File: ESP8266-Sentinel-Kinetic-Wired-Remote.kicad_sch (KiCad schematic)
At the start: 41 parts, among them J1 Conn_01x04_Socket, SW1 SW_Push, SW2 SW_Push, SW3 SW_Push, SW4 SW_Push, SW5 SW_Push, U1 AMS1117-3.3, U2 ESP-12F

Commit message: Layed out PCB and created 3D printable enclosure
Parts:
- removed DS?: WC1602A, Display:LCD-016N002L, symbol Display_Character:WC1602A
- added DS1: WC1602A, Display:WC1602A, symbol Display_Character:WC1602A
- added H1, H2, H3, H4: MountingHole, MountingHole:MountingHole_3.2mm_M3, symbol Mechanical:MountingHole
- added RV2: 5K, Potentiometer_THT:Potentiometer_ACP_CA14V-15_Vertical, symbol Device:R_Potentiometer
- J1: now not fitted; now left out of the parts list
- J3: renamed from J?; now not fitted; now left out of the parts list
- RV1: renamed from RV?; footprint Potentiometer_THT:Potentiometer_ACP_CA14V-15_Vertical -> Potentiometer_THT:Potentiometer_Runtron_RM-065_Vertical
- gave numbers to parts that had none: 6
- renumbered SW4 to SW1, SW1 to SW4
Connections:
- net +5V: now also J2.1 (Pin_1), DS1.2 (VDD), RV2.1
- net GND: now also J2.4 (Pin_4), DS1.1 (VSS), RV2.3
- net RS232_RX: now also J2.2 (Pin_2)
- net RS232_TX: now also J2.3 (Pin_3)
- net at U4.16 (P4): now also DS1.11 (D4)
- net at U4.17 (P5): now also DS1.12 (D5)
- net at U4.19 (P6): now also DS1.13 (D6)
- net at U4.20 (P7): now also DS1.14 (D7)
- net at JP4.1 (A): now also DS1.15 (LED(+))
- net at Q1.3 (D): now also DS1.16 (LED(-))
- net at RV1.2: now also DS1.3 (VO), RV2.2
- net at U4.10 (P0): now also DS1.4 (RS)
- net at U4.11 (P1): now also DS1.5 (R/W)
- net at U4.12 (P2): now also DS1.6 (E)
- net A0: no longer names the net of U2.2 (ADC)
- net GPIO16: no longer names the net of U2.4 (GPIO16)
- no-connect marks 13 -> 15

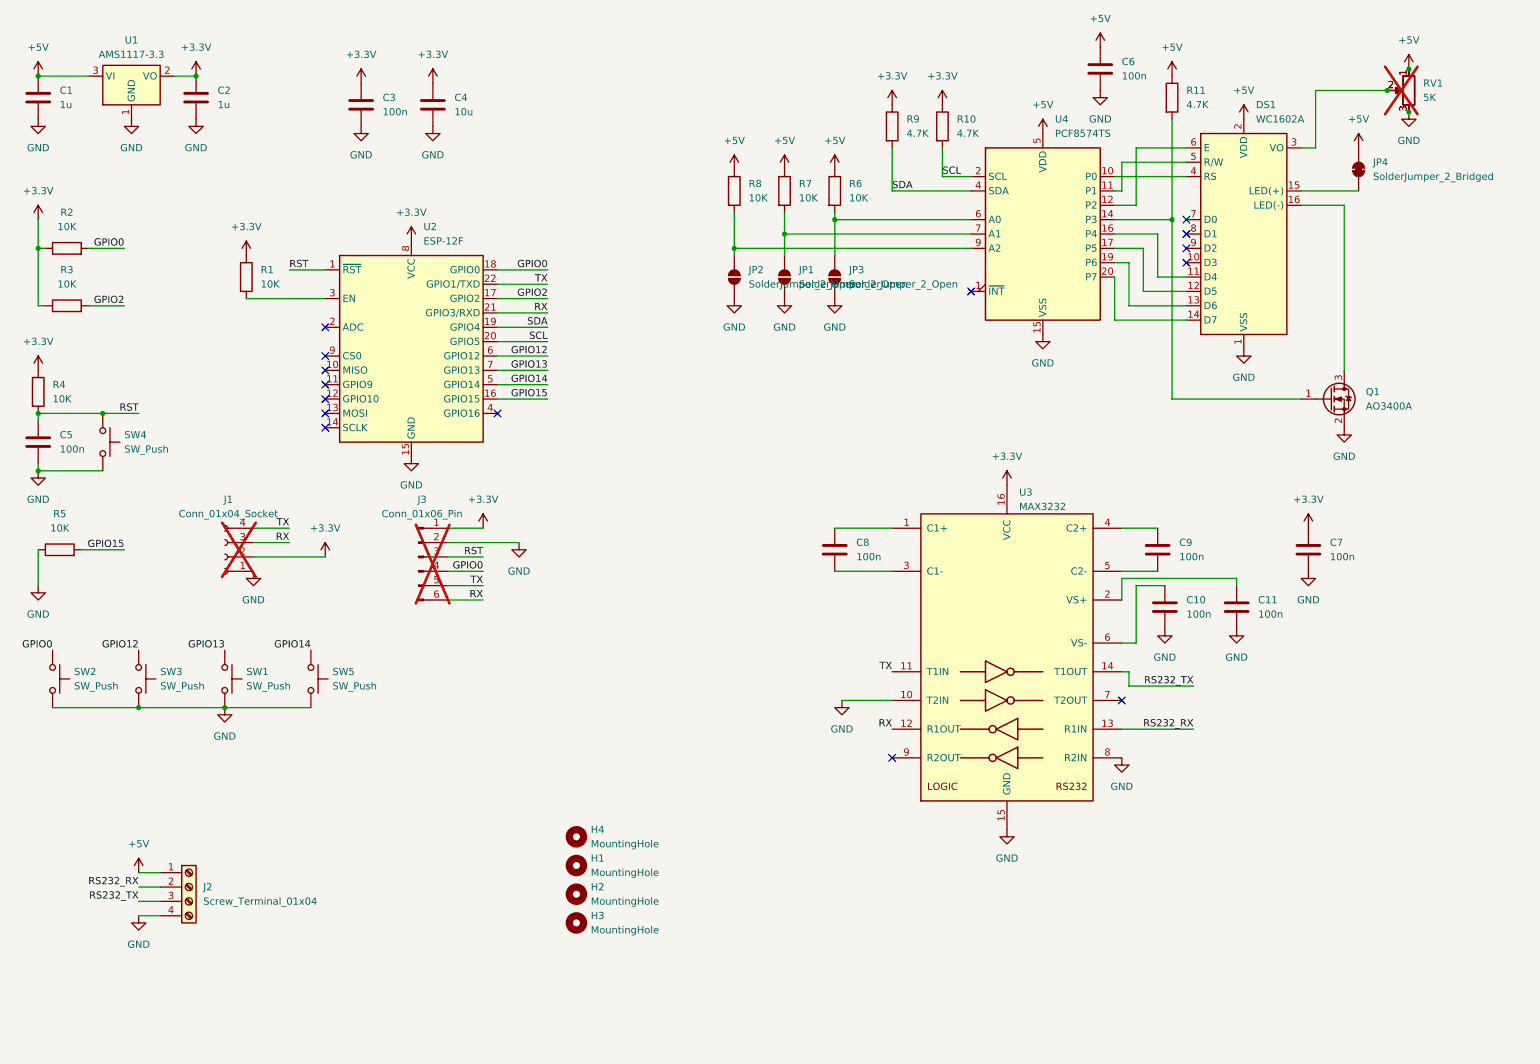
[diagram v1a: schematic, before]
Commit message: Added JLCPCB part numbers Rotated programming ports
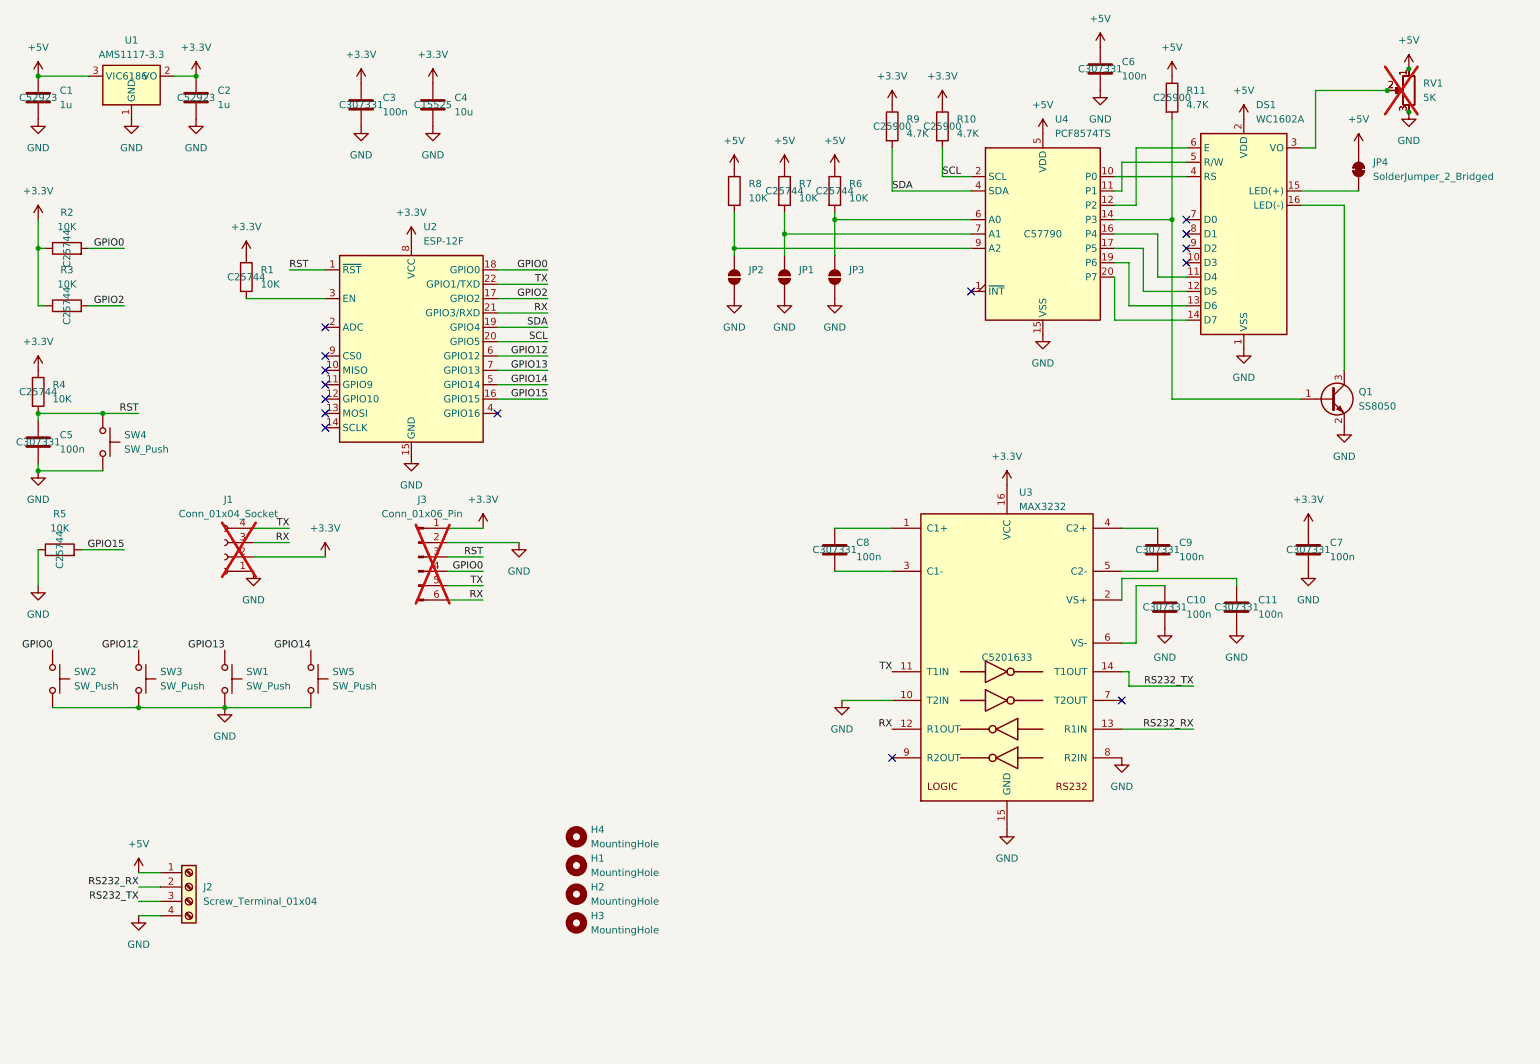
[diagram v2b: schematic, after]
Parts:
- removed Q1: AO3400A, Package_TO_SOT_SMD:SOT-23, symbol Transistor_FET:AO3400A
- added Q1: SS8050, Package_TO_SOT_SMD:SOT-23, symbol Transistor_BJT:SS8050
- C1, C2: LCSC (none) -> C52923
- C10, C11, C3, C5, C6, C7, C8, C9: LCSC (none) -> C307331
- C4: LCSC (none) -> C15525
- R1, R2, R3, R4, R5, R6, R7, R8: LCSC (none) -> C25744
- R10, R11, R9: LCSC (none) -> C25900
- U1: LCSC (none) -> C6186
- U3: LCSC (none) -> C5201633
- U4: LCSC (none) -> C57790
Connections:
- net GND: now also Q1.2 (E)
- net at R11.2, U4.14 (P3): now also Q1.1 (B)
- net at DS1.16 (LED(-)): now also Q1.3 (C)

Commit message: Add JLCPCB part number for SS8050 Remove panel creation action
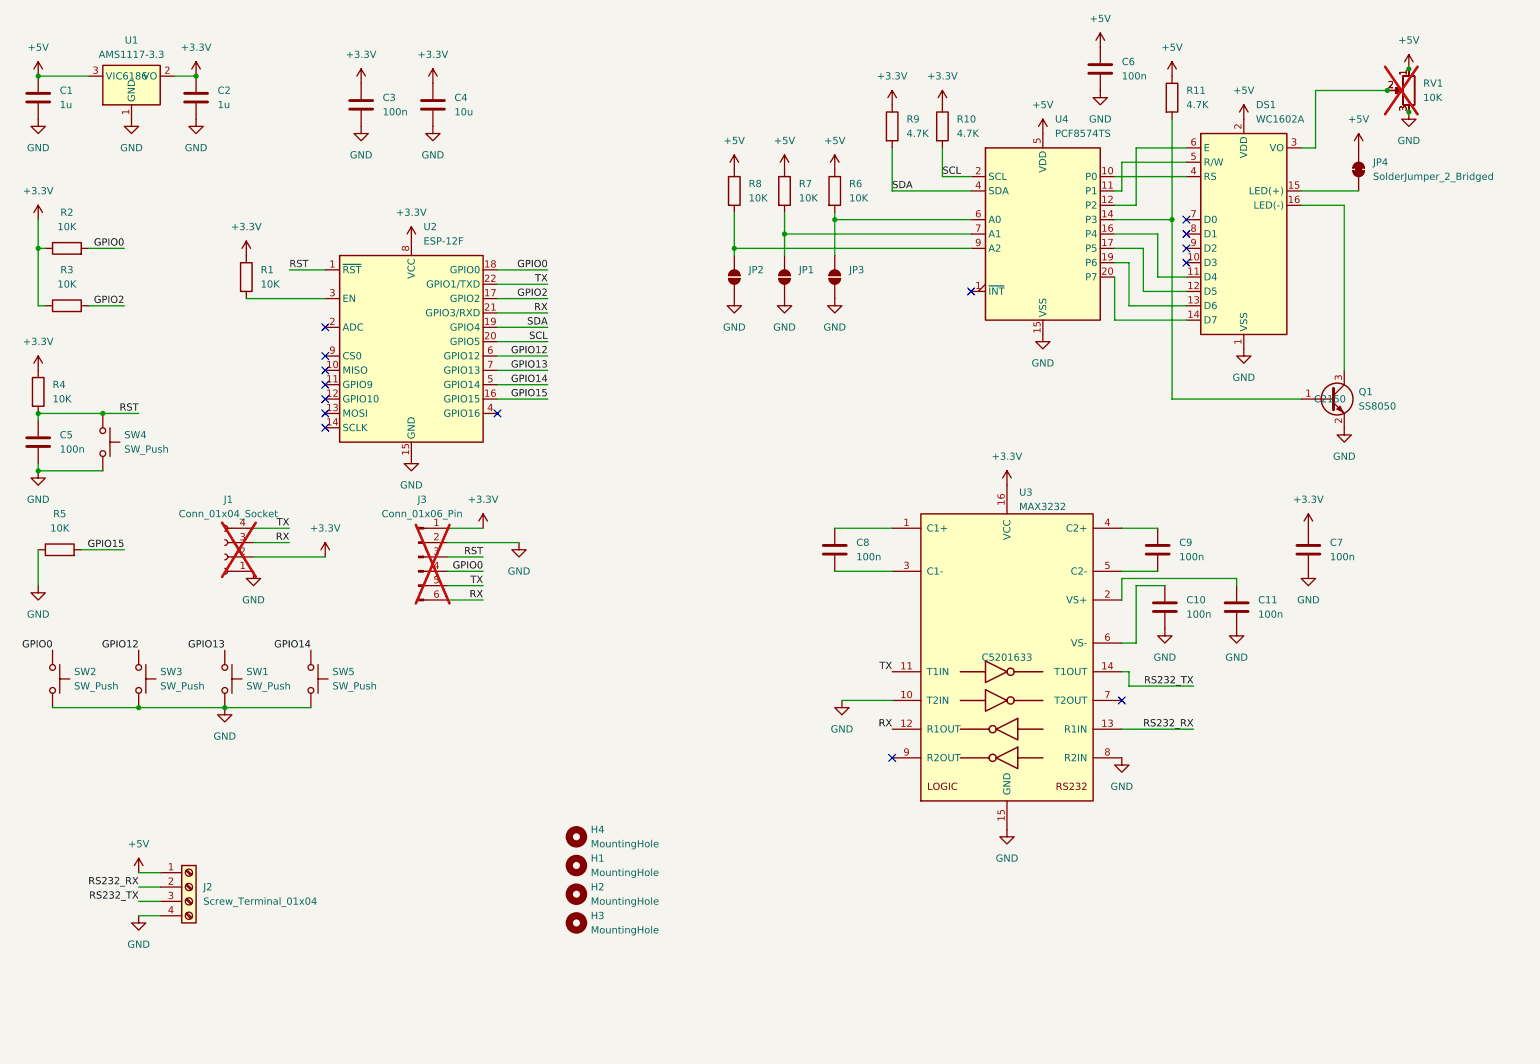
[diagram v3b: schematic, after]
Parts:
- DS1, J2, SW1, SW2, SW3, SW4, SW5: now left out of the parts list
- Q1: LCSC (none) -> C2150
- RV1: value 5K -> 10K; now left out of the parts list
- RV2: value 5K -> 10K
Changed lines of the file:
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@@
 					(size 1.27 1.27)
 				)
+				(hide yes)
 			)
 		)
@@
 					(size 1.27 1.27)
 				)
+				(hide yes)
 			)
 		)
@@
 		(unit 1)
 		(exclude_from_sim no)
-		(in_bom yes)
+		(in_bom no)
 		(on_board yes)
 		(dnp no)
@@
 					(size 1.27 1.27)
 				)
+				(hide yes)
 			)
 		)
@@
 		(unit 1)
 		(exclude_from_sim no)
-		(in_bom yes)
+		(in_bom no)
 		(on_board yes)
 		(dnp no)
@@
 					(size 1.27 1.27)
 				)
+				(hide yes)
 			)
 		)
@@
 					(size 1.27 1.27)
 				)
+				(hide yes)
 			)
 		)
@@
 			)
 		)
-		(property "Value" "5K"
+		(property "Value" "10K"
 			(at 265.43 27.9399 0)
 			(effects
@@
 					(size 1.27 1.27)
 				)
+				(hide yes)
 			)
 		)
@@
 		(unit 1)
 		(exclude_from_sim no)
-		(in_bom yes)
+		(in_bom no)
 		(on_board yes)
 		(dnp no)
@@
 					(size 1.27 1.27)
 				)
+				(hide yes)
 			)
 		)
@@
 		(unit 1)
 		(exclude_from_sim no)
-		(in_bom yes)
+		(in_bom no)
 		(on_board yes)
 		(dnp no)
@@
 					(size 1.27 1.27)
 				)
+				(hide yes)
 			)
 		)
@@
 					(size 1.27 1.27)
 				)
+				(hide yes)
 			)
 		)
@@
 					(size 1.27 1.27)
 				)
+				(hide yes)
 			)
 		)
@@
 					(size 1.27 1.27)
 				)
+				(hide yes)
 			)
 		)
@@
 					(size 1.27 1.27)
 				)
+				(hide yes)
 			)
 		)
@@
 					(size 1.27 1.27)
 				)
+				(hide yes)
 			)
 		)
@@
 					(size 1.27 1.27)
 				)
+				(hide yes)
 			)
 		)
@@
 					(size 1.27 1.27)
 				)
+				(hide yes)
 			)
 		)
@@
 					(size 1.27 1.27)
 				)
+				(hide yes)
 			)
 		)
@@
 					(size 1.27 1.27)
 				)
+				(hide yes)
 			)
 		)
@@
 			)
 		)
+		(property "LCSC" "C2150"
+			(at 248.92 81.28 0)
+			(effects
+				(font
+					(size 1.27 1.27)
+				)
+			)
+		)
 		(pin "2"
 		)
@@
 					(size 1.27 1.27)
 				)
+				(hide yes)
 			)
 		)
@@
 					(size 1.27 1.27)
 				)
+				(hide yes)
 			)
 		)
@@
 		(unit 1)
 		(exclude_from_sim no)
-		(in_bom yes)
+		(in_bom no)
 		(on_board yes)
 		(dnp no)
@@
 					(size 1.27 1.27)
 				)
+				(hide yes)
 			)
 		)
@@
 		(unit 1)
 		(exclude_from_sim no)
-		(in_bom yes)
+		(in_bom no)
 		(on_board yes)
 		(dnp no)
@@
 			)
 		)
-		(property "Value" "5K"
+		(property "Value" "10K"
 			(at 265.43 27.9399 0)
 			(effects
@@
 		(unit 1)
 		(exclude_from_sim no)
-		(in_bom yes)
+		(in_bom no)
 		(on_board yes)
 		(dnp no)
@@
 		(unit 1)
 		(exclude_from_sim no)
-		(in_bom yes)
+		(in_bom no)
 		(on_board yes)
 		(dnp no)
@@
 					(size 1.27 1.27)
 				)
+				(hide yes)
 			)
 		)
@@
 					(size 1.27 1.27)
 				)
+				(hide yes)
 			)
 		)

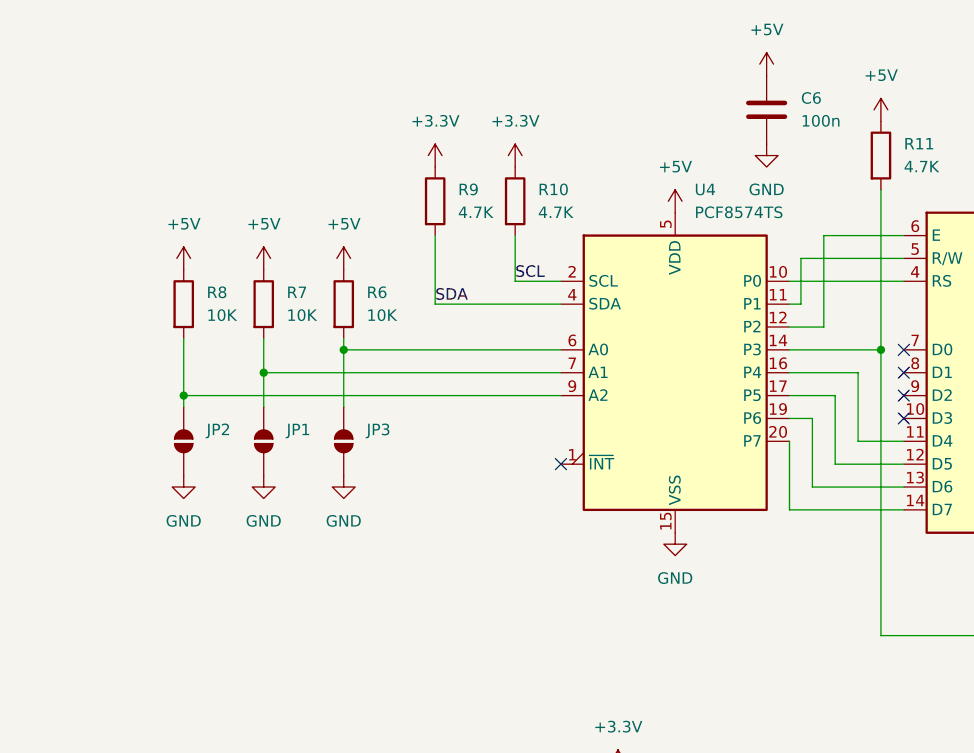
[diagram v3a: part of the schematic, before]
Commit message: Replaced PCF8574 package
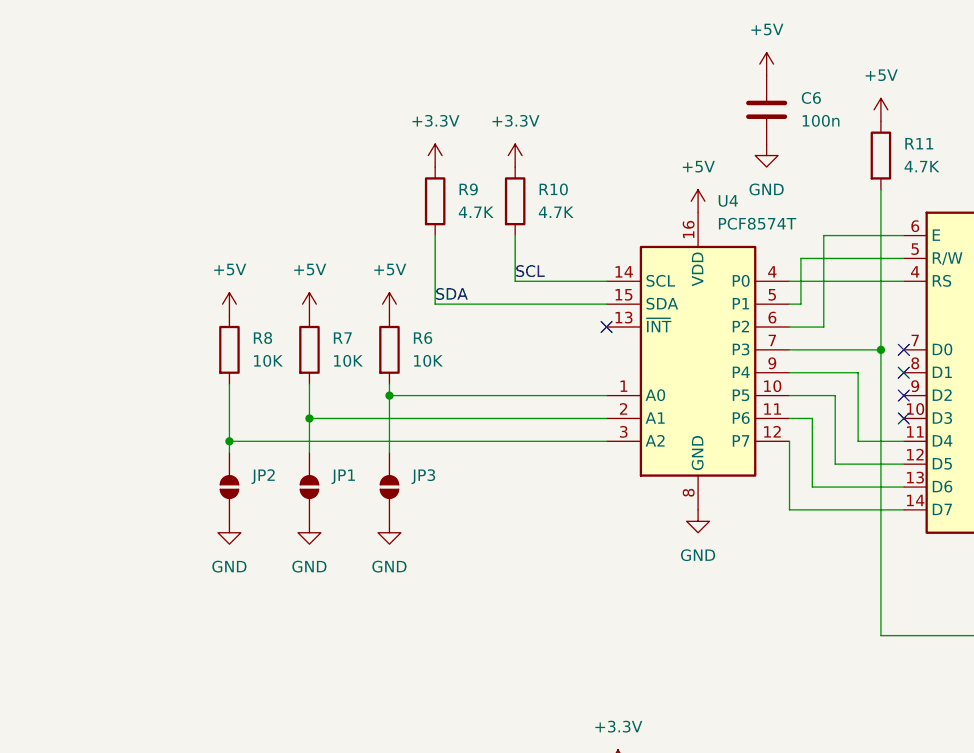
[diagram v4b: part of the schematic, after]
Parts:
- removed U4: PCF8574TS, Package_SO:SSOP-20_4.4x6.5mm_P0.65mm, symbol Interface_Expansion:PCF8574TS
- added U4: PCF8574T, Package_SO:SOIC-16_3.9x9.9mm_P1.27mm, symbol Interface_Expansion:PCF8574T
- U2: now left out of the parts list
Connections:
- net +5V: now also U4.16 (VDD)
- net GND: now also U4.8 (GND)
- net SCL: now also U4.14 (SCL)
- net SDA: now also U4.15 (SDA)
- net at Q1.1 (B), R11.2: now also U4.7 (P3)
- net at DS1.4 (RS): now also U4.4 (P0)
- net at DS1.5 (R/W): now also U4.5 (P1)
- net at DS1.6 (E): now also U4.6 (P2)
- net at DS1.11 (D4): now also U4.9 (P4)
- net at DS1.12 (D5): now also U4.10 (P5)
- net at DS1.13 (D6): now also U4.11 (P6)
- net at DS1.14 (D7): now also U4.12 (P7)
- net at JP3.2 (B), R6.2: now also U4.1 (A0)
- net at JP1.2 (B), R7.2: now also U4.2 (A1)
- net at JP2.2 (B), R8.2: now also U4.3 (A2)
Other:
- moved on the sheet: JP1, JP2, JP3, R6, R7, R8

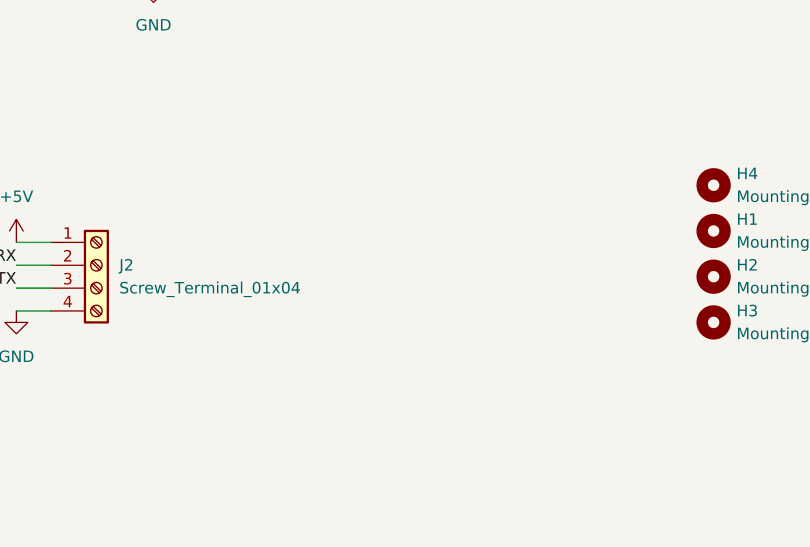
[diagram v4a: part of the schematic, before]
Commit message: Added TVS diodes for protection
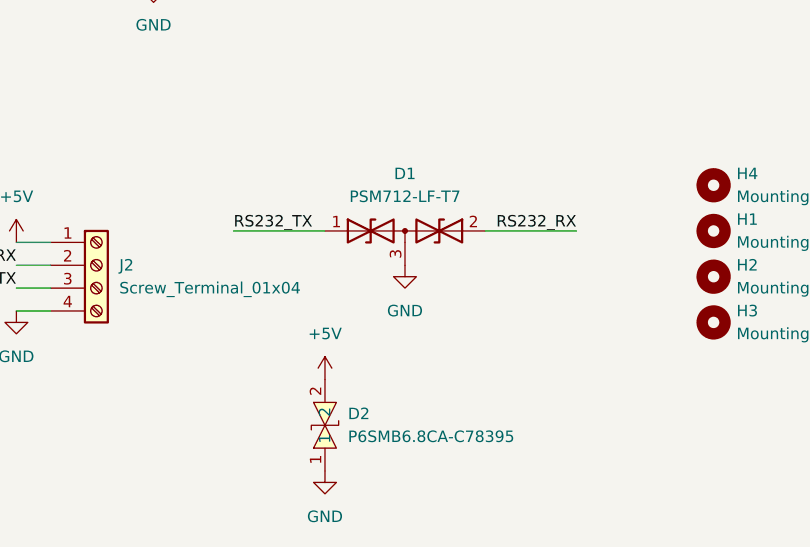
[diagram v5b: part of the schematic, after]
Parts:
- added D1: PSM712-LF-T7, Package_TO_SOT_SMD:SOT-23, symbol Device:D_TVS_Dual_AAC
- added D2: P6SMB6.8CA-C78395, lib:SMB_L4.6-W3.6-LS5.3-BI, symbol lib:P6SMB6.8CA-C78395
- U3: footprint Package_SO:TSSOP-16_4.4x5mm_P0.65mm -> Package_SO:SOP-16_3.9x9.9mm_P1.27mm
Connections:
- net +5V: now also D2.2
- net GND: now also D1.3 (common), D2.1
- net RS232_RX: now also D1.2 (A2)
- net RS232_TX: now also D1.1 (A1)
